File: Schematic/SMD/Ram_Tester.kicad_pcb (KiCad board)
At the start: 2 copper layers, 38.7 x 59 mm, 35 parts, among them J1 Conn_01x04_Pin, J2 ICSP, J3 USB_C_Receptacle_PowerOnly_6P, Q1 IRLML6402, Q2 IRLML6402, SW1 SW_DIP_x03, SW2 SW_Push, U1 ATmega328-P, U2 RAM / ZIF, U3 ZIP Socket, U4 DIP Socket, Y1 Crystal

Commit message: v1.1 of Board
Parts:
- removed U4: DIP Socket, Package_DIP:DIP-20_W7.62mm
- C4, C7, R3, R4, R5: moved to F.Cu
- D1: value LED_Dual_AAK -> LED_Dual_AAKK; footprint LED_SMD:LED_SMD_RG_AKAK -> LED_SMD:LED_RGB_Wuerth_150080M153000
- Q1, Q2: value IRLML6402 -> BSS138
- SW1: footprint Package_DIP:DIP-6_W7.62mm -> Button_Switch_THT:SW_DIP_SPSTx03_Slide_9.78x9.8mm_W7.62mm_P2.54mm
- moved RN2 24.6 mm to (114.4, 109.8)
- moved R7 14.1 mm to (123.8, 94.8)
- moved R5 11.0 mm to (110.9, 95.3)
- moved R4 8.96 mm to (110.9, 97.0)
- moved R3 7.85 mm to (110.9, 98.5)
- moved Q1 7.79 mm to (131.5, 66.4), turned to 0 degrees
- moved RN3 6.99 mm to (123.8, 87.3)
- moved RN1 6.43 mm to (123.8, 91.8)
- moved C4 4.92 mm to (109.2, 111.0), turned to 180 degrees
- moved RN4 4.26 mm to (136.9, 76.6)
- moved C2 3.70 mm to (110.9, 92.4)
- moved R1 3.18 mm to (137.0, 65.5)
- moved C3 2.96 mm to (107.8, 92.4)
- moved Y1 2.96 mm to (109.7, 89.7)
- moved Q2 2.70 mm to (131.4, 70.0), turned to 0 degrees
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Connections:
- C4 pad 1: /GND2 -> /GND
- C4 pad 2: /5V2 -> Net-(U1-PC5)
- D1 pad 1: Net-(D1-A1) -> /5V
- D1 pad 2: Net-(D1-A2) -> /5V
- D1 pad 3: /GND -> Net-(D1-K1)
- D1 pad 4: /GND -> Net-(D1-K2)
- Q1 pad 2: Net-(Q1-S) -> /GND
- Q1 pad 3: /5V -> Net-(Q1-D)
- Q2 pad 2: Net-(Q2-S) -> /GND
- Q2 pad 3: /5V -> Net-(Q2-D)
- R1 pad 1: Net-(D1-A1) -> Net-(D1-K2)
- R1 pad 2: Net-(Q1-S) -> Net-(Q1-D)
- R4 pad 2: Net-(RN3-R4.1) -> Net-(J2-Pin_4)
- R6 pad 1: Net-(Q2-S) -> Net-(Q2-D)
- R6 pad 2: Net-(D1-A2) -> Net-(D1-K1)
- RN3 pad 4: Net-(RN3-R4.1) -> Net-(J2-Pin_4)
- SW1 pad 5: Net-(RN3-R4.1) -> Net-(J2-Pin_4)
- U2 pad 9: Net-(RN3-R4.1) -> Net-(J2-Pin_4)
- U3 pad 1: Net-(U3-OE) -> Net-(RN1-R2.1)
- U3 pad 10: Net-(U3-N/C) -> Net-(U2-N/C)
- U3 pad 11: Net-(U3-A0) -> Net-(RN3-R1.1)
- U3 pad 12: Net-(U3-A1) -> Net-(RN3-R2.1)
- U3 pad 13: Net-(U3-A2) -> Net-(RN3-R3.1)
- U3 pad 14: Net-(U3-A3) -> Net-(J2-Pin_4)
- U3 pad 15: /5V2 -> Net-(U1-PC5)
- U3 pad 16: Net-(U3-A4) -> Net-(RN2-R4.1)
- U3 pad 17: Net-(U3-A5) -> Net-(RN2-R3.1)
- U3 pad 18: Net-(U3-A6) -> Net-(RN2-R2.1)
- U3 pad 19: Net-(U3-A7) -> Net-(RN2-R1.1)
- U3 pad 2: Net-(U3-CAS) -> Net-(RN1-R4.1)
- U3 pad 20: Net-(U3-A8) -> Net-(U2-A8)
- U3 pad 3: Net-(U3-I/O3) -> Net-(RN4-R2.1)
- U3 pad 4: Net-(U3-I/O4) -> Net-(RN4-R1.1)
- U3 pad 5: /GND2 -> /GND
- U3 pad 6: Net-(U3-I/O1) -> Net-(RN4-R4.1)
- U3 pad 7: Net-(U3-I/O2) -> Net-(RN4-R3.1)
- U3 pad 8: Net-(U3-WE) -> Net-(J2-Pin_4)
- U3 pad 9: Net-(U3-RAS) -> Net-(RN1-R3.1)
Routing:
- net Net-(RN4-R1.1): track 5.60 -> 89.2 mm
- net Net-(RN1-R4.1): track 11.2 -> 81.1 mm
- net Net-(RN4-R2.1): track 8.47 -> 76.5 mm
- net Net-(RN4-R4.1): track 3.73 -> 65.3 mm, vias 0 -> 2
- net Net-(RN4-R3.1): track 6.09 -> 60.3 mm
- net Net-(RN2-R3.1): track 2.73 -> 48.6 mm
- net Net-(U1-PC5): track 60.3 -> 104.9 mm, vias 2 -> 4
- net Net-(RN2-R1.1): track 4.33 -> 48.5 mm
- net Net-(RN1-R2.1): track 20.7 -> 63.3 mm, vias 0 -> 3
- net Net-(RN2-R2.1): track 3.03 -> 43.7 mm
- net Net-(RN3-R4.1): track 37.2 -> 0.00 mm, vias 1 -> 0
- net Net-(J2-Pin_4): track 56.0 -> 93.2 mm, vias 2 -> 1
- net Net-(U2-A8): track 2.21 -> 38.8 mm
- net Net-(RN2-R4.1): track 5.02 -> 40.1 mm
- net Net-(U2-N/C): track 16.4 -> 51.3 mm, vias 1 -> 3
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- removed copper zone on B.Cu, net /GND2
- removed copper zone on F.Cu, net /GND2
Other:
- board size 38.7 x 59 mm -> 39 x 59.4 mm
- board text added: "Ram Align —>"
- board text added: "ZIF⇒"
- board text added: "ZIP Socket OR ZIF Socket! Not both!"
- board text added: "ZIP(19/20Pin)↓↓"
- board text removed: "Lower Side Towards ZIF"
- board text removed: "Ram Align ———>"
- board text removed: "ZIP Adapter"

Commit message: V1.0 fixed
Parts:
- C1, C4, C7: footprint Capacitor_SMD:C_0805_2012Metric -> Capacitor_SMD:C_0603_1608Metric_Pad1.08x0.95mm_HandSolder
- D1: footprint LED_SMD:LED_RGB_Wuerth_150080M153000 -> LED_SMD:LED_SMD_RG_AKAK
- F1: value Fuse -> 0.5A
- R1: value 100 -> 150
- R6: value 150 -> 330
- SW1: footprint Button_Switch_THT:SW_DIP_SPSTx03_Slide_9.78x9.8mm_W7.62mm_P2.54mm -> Package_DIP:DIP-6_W7.62mm
- Y1: value Crystal -> 16MHZ
- moved C1 0.65 mm to (107.9, 80.6), turned to 90 degrees
- moved D1 0.40 mm to (141.1, 66.5), turned to 180 degrees
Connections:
- Q1 pad 1: Net-(J1-Pin_4) -> Net-(J1-Pin_3)
- Q2 pad 1: Net-(J1-Pin_3) -> Net-(J1-Pin_4)
- R4 pad 2: Net-(J2-Pin_4) -> Net-(RN3-R4.1)
- RN1 pad 1: Net-(J2-Pin_4) -> Net-(RN1-R1.1)
- RN1 pad 8: Net-(RN1-R1.2) -> Net-(J2-Pin_4)
- RN3 pad 4: Net-(J2-Pin_4) -> Net-(RN3-R4.1)
- SW1 pad 5: Net-(J2-Pin_4) -> Net-(RN3-R4.1)
- U1 pad 15: Net-(RN1-R1.2) -> Net-(J2-Pin_4)
- U1 pad 22: /GND -> /5V
- U2 pad 3: Net-(J2-Pin_4) -> Net-(RN1-R1.1)
- U2 pad 9: Net-(J2-Pin_4) -> Net-(RN3-R4.1)
- U3 pad 14: Net-(J2-Pin_4) -> Net-(RN3-R4.1)
- U3 pad 8: Net-(J2-Pin_4) -> Net-(RN1-R1.1)
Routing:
- net Net-(RN3-R4.1): track 0.00 -> 62.3 mm
- net Net-(J2-Pin_4): track 93.2 -> 31.1 mm, vias 1 -> 3
- net Net-(RN1-R1.1): track 0.00 -> 58.3 mm, vias 0 -> 3
- net Net-(RN1-R1.2): track 12.0 -> 0.00 mm, vias 1 -> 0
- net /5V: track 127.8 -> 116.7 mm
- net /GND: track 188.1 -> 192.8 mm, vias 55 -> 47
- net Net-(J1-Pin_4): track 66.8 -> 62.4 mm
- net Net-(RN4-R4.1): track 65.3 -> 68.3 mm
- net Net-(U2-N/C): track 51.3 -> 48.6 mm
- net Net-(RN3-R2.1): track 41.9 -> 39.6 mm
- net Net-(RN4-R3.1): track 60.3 -> 61.9 mm
- net Net-(RN2-R1.1): track 48.5 -> 49.6 mm
- net Net-(RN3-R1.1): track 44.5 -> 43.6 mm
- net Net-(RN3-R3.1): track 66.0 -> 65.2 mm
- net Net-(RN2-R4.2): track 40.1 -> 40.8 mm
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
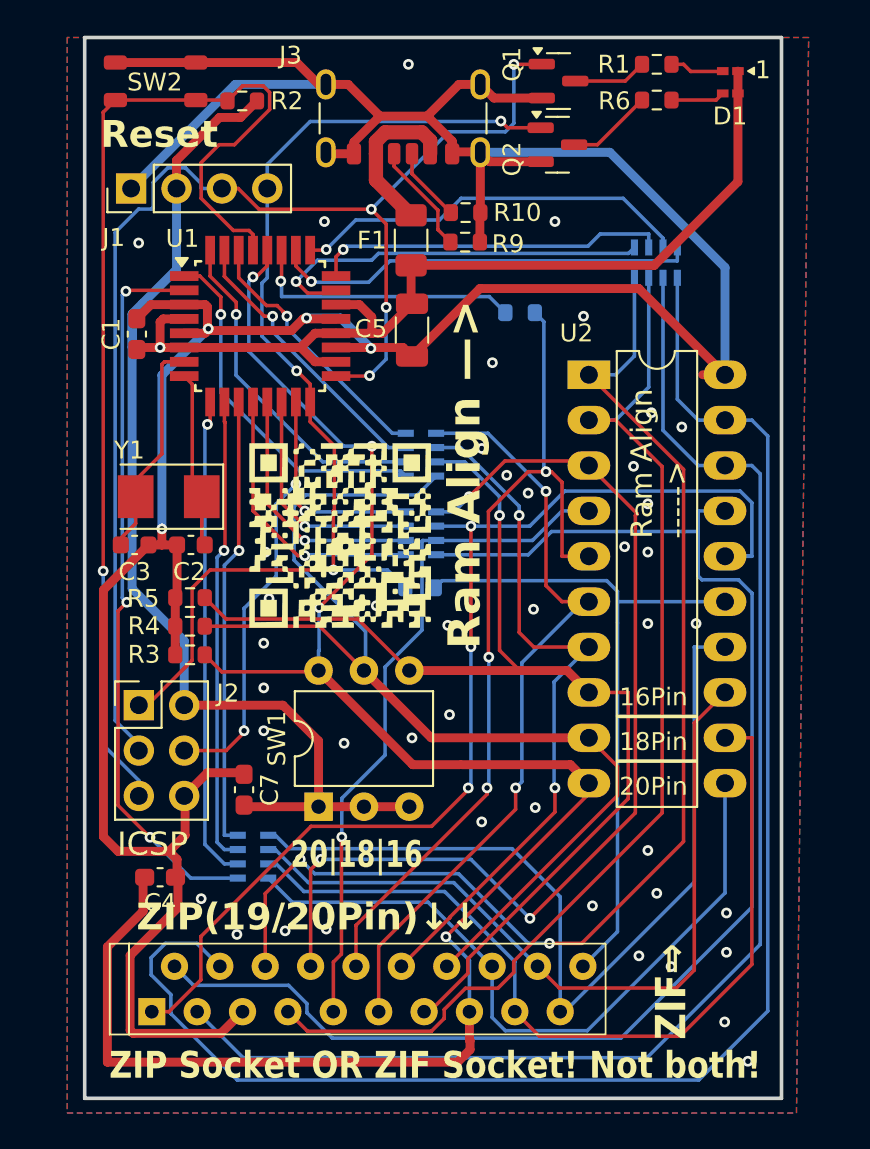
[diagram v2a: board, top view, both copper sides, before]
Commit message: v2.1 of SMD
Some adjustmens to allow more space for the 0.96" OLED Display
Minor Footprint Adjustments for 0605 DUO Led
Fixed wrong Track Size for ZIP 5V Power Supply
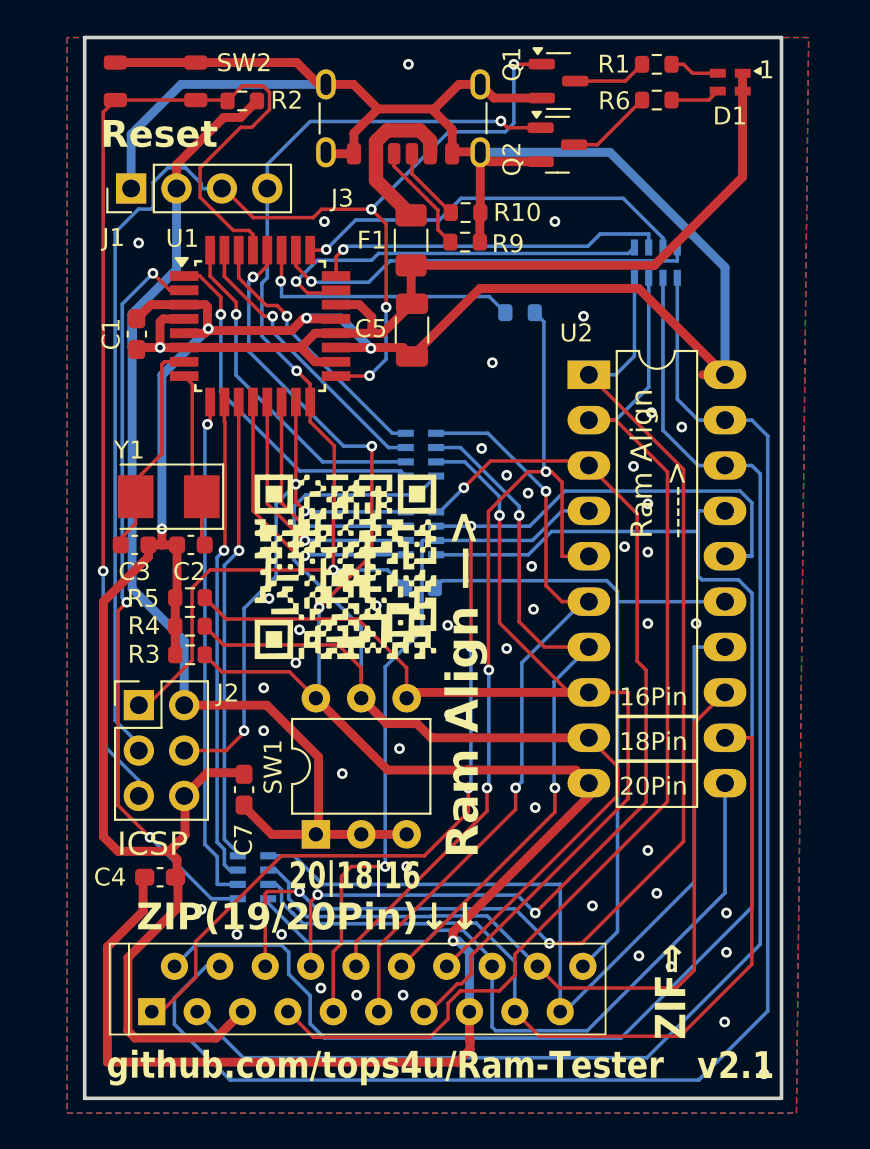
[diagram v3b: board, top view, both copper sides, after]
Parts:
- D1: value LED_Dual_AAKK -> VS 3JD8
- J3: value USB_C_Receptacle_PowerOnly_6P -> KUSBX-SMT-CS-6-BTR
- R1: value 150 -> 150R
- R6: value 330 -> 470R
- R7, R8, RN1, RN2, RN3, RN4: value 47 -> 47R
- moved G*** 1.78 mm to (119.6, 93.6)
- moved SW1 1.56 mm to (117.9, 108.6)
- moved RN2 1.15 mm to (114.4, 111.0)
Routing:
- net Net-(RN4-R1.1): track 89.7 -> 85.7 mm
- net Net-(RN3-R3.1): track 65.2 -> 68.1 mm
- net Net-(RN1-R1.1): track 58.3 -> 55.5 mm
- net /GND: track 192.8 -> 195.2 mm, vias 47 -> 52
- net Net-(RN1-R4.1): track 81.1 -> 83.5 mm
- net Net-(RN4-R4.1): track 68.3 -> 66.8 mm
- net /5V: track 116.7 -> 118.2 mm
- net Net-(RN2-R3.2): track 27.2 -> 28.6 mm
- net Net-(RN3-R4.1): track 62.3 -> 63.7 mm
- net Net-(RN1-R3.1): track 38.4 -> 39.5 mm
- net Net-(U1-PC5): track 104.8 -> 105.8 mm
- net Net-(RN2-R2.2): track 26.2 -> 27.1 mm
- net Net-(RN2-R4.2): track 40.8 -> 41.8 mm
- net Net-(RN4-R3.1): track 61.9 -> 62.8 mm
- net Net-(RN2-R4.1): track 40.1 -> 40.9 mm
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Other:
- board text added: "v2.1"
- board text removed: "ZIP Socket OR ZIF Socket! Not both!"

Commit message: v2.1 Update
Minor Text modifications
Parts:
- SW1: footprint Package_DIP:DIP-6_W7.62mm -> Button_Switch_THT:SW_DIP_SPSTx03_Slide_9.78x9.8mm_W7.62mm_P2.54mm
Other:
- board text added: "20 18 16"
- board text removed: "20|18|16"
